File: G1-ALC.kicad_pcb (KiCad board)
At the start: 2 copper layers, 100 x 100.1 mm, 89 parts, among them J101 Conn_01x03_Pin, J102 330 VAC In, J103 G1 connections, J104 105VAC in, J105 Conn_01x03_Pin, J107 Conn_01x05_Pin, J108 G2 Control board interconnect, Q101 TIP122, U101 LM7812_TO220, U102 LM324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

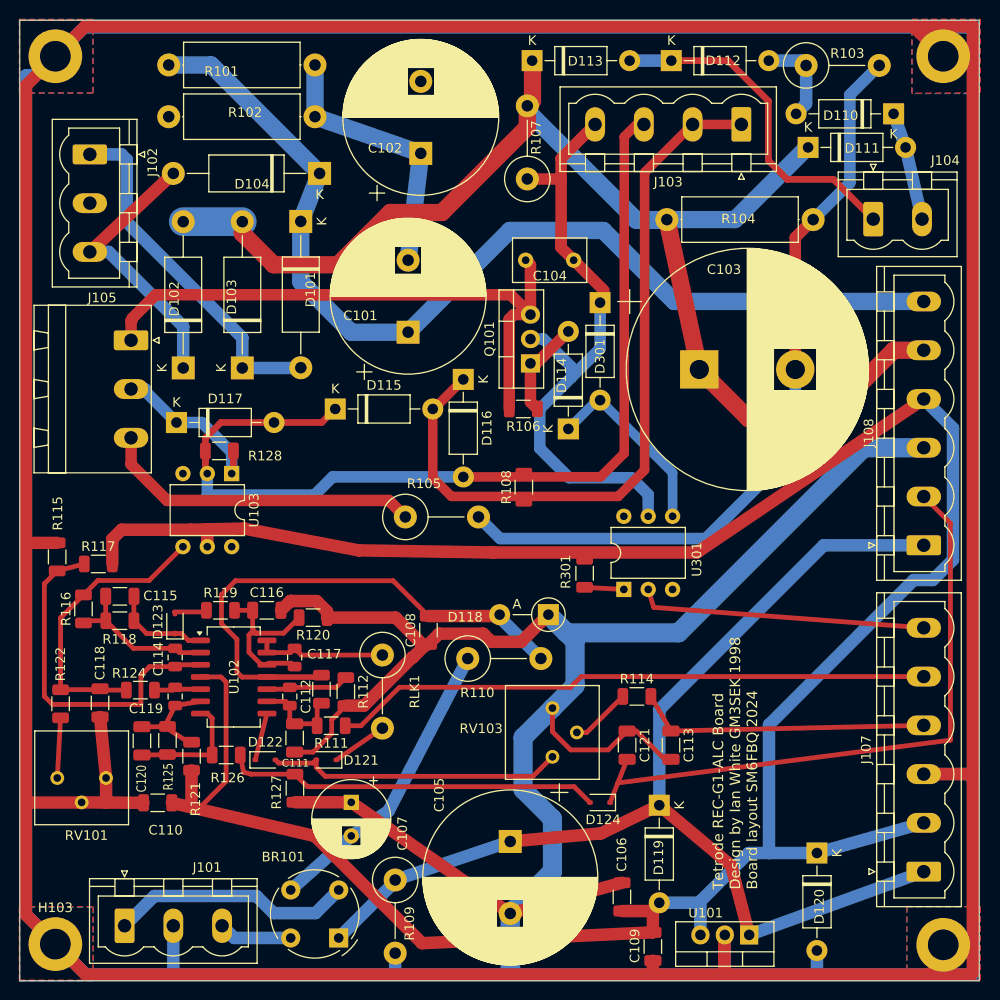
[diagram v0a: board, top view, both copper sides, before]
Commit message: Fixes for issues #1, #2, #3 and #4
Fixed unconnected capacitor and bleeder
Turned connectors around to orient screw connectors with screws outward from the board.
Use new footprint for BY228 diodes with larget pand and holes.
Moved components to make more room for the Q101 heat sink.
Cleared the top copper layer below the Q101 heat sink forn connected traces.
Added a copper zone below the Q101 heat sink to make it possible to solder the heat sink onto the board.
Opened the solder mask below the heat sink.

Added danger zones on both silkscreen layers. Along with warning texts.
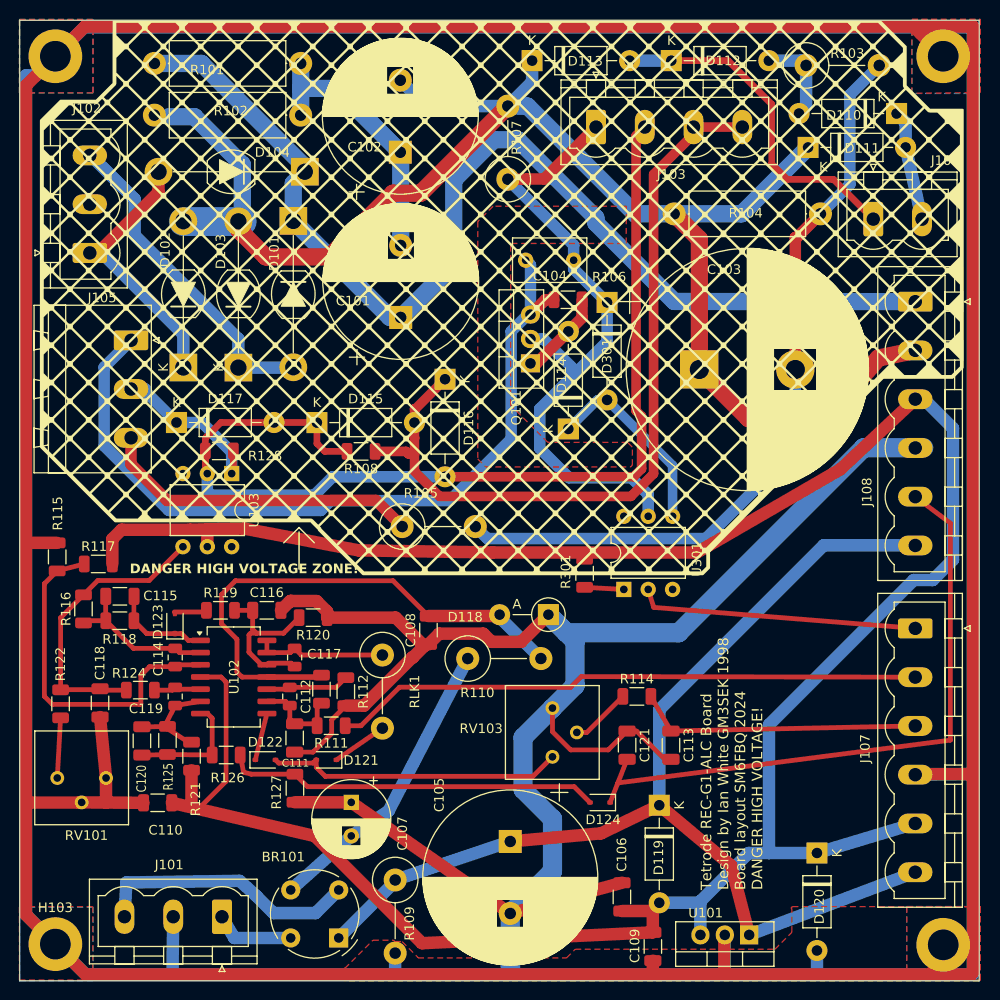
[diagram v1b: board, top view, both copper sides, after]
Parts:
- D101, D102, D103, D104: footprint Diode_THT:D_DO-15_P15.24mm_Horizontal -> Diode_THT_AKL:D_SOD-64_P15.24mm_big_holes_Horizontal
- moved J108 25.4 mm to (143.3, 54.3), turned to -90 degrees
- moved J107 25.4 mm to (143.3, 88.4), turned to -90 degrees
- moved R108 17.4 mm to (85.6, 69.9), turned to 180 degrees
- moved J103 15.1 mm to (110.1, 36.1), turned to 0 degrees
- moved R106 12.3 mm to (107.2, 54.1)
- moved J102 10.3 mm to (57.3, 49.2), turned to 90 degrees
- moved J101 10.2 mm to (71.1, 118.4), turned to 180 degrees
- moved D115 2.38 mm to (81.0, 66.9)
- moved C102 2.13 mm to (89.7, 38.8)
- moved R107 2.03 mm to (100.9, 41.6)
- moved D116 1.90 mm to (94.3, 62.4)
- moved C101 1.72 mm to (89.7, 56.0)
- moved R101 1.50 mm to (64.1, 29.5)
- moved D104 1.50 mm to (79.8, 40.8)
- moved R102 1.50 mm to (79.3, 34.9)
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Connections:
- C102 pad 2: unconnected-(C102-Pad2) -> /Cathode
- J101 pad 1: /18 VAC - -> /18 VAC +
- J101 pad 3: /18 VAC + -> /18 VAC -
- J102 pad 1: /330VAC - -> /330VAC +
- J102 pad 3: /330VAC + -> /330VAC -
- J103 pad 1: /G1 meter - -> /G1 Switch
- J103 pad 2: /G1 meter - -> /G1 meter +
- J103 pad 3: /G1 meter + -> /G1 meter -
- J103 pad 4: /G1 Switch -> /G1 meter -
- J107 pad 1: +24V -> Class AB1_L
- J107 pad 2: +12V -> INH IN
- J107 pad 3: GNDPWR -> ALC Out
- J107 pad 4: ALC Out -> GNDPWR
- J107 pad 5: INH IN -> +12V
- J107 pad 6: Class AB1_L -> +24V
- J108 pad 1: +24V -> /G2-Unreg
- J108 pad 2: /G1 current trip -> /Cathode
- J108 pad 3: GNDPWR -> +12V
- J108 pad 4: +12V -> GNDPWR
- J108 pad 5: /Cathode -> /G1 current trip
- J108 pad 6: /G2-Unreg -> +24V
- R102 pad 2: unconnected-(R102-Pad2) -> /Cathode
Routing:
- net /Cathode: track 136.7 -> 161.5 mm
- net /RV102 Cold: track 63.2 -> 83.1 mm
- net /G2-Unreg: track 106.6 -> 114.8 mm
- net /G1 meter +: track 101.6 -> 107.3 mm
- net /G1 meter -: track 78.7 -> 84.4 mm
- net /G1 Switch: track 64.1 -> 68.8 mm
- net /18 VAC -: track 25.3 -> 28.0 mm
- net /330VAC -: track 36.8 -> 34.3 mm
- net /330VAC +: track 29.2 -> 27.7 mm
- net +12V: track 267.5 -> 266.1 mm
- net GNDPWR: track 1030.2 -> 1031.6 mm
- net Net-(D114-A): track 10.4 -> 9.21 mm
- net ALC Out: track 30.5 -> 29.6 mm
- net INH IN: track 62.4 -> 61.5 mm
- net Class AB1_L: track 30.2 -> 29.3 mm
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- added copper zone on F.Cu, net (none)
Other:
- board text added: "DANGER HIGH VOLTAGE ZONE!"
- board text added: "DANGER! HIGH VOLTAGE ZONE"
- board text added: "Tetrode REC-G1-ALC Board Design by Ian White GM3SEK 1998 Board layout SM6FBQ 2024 DANGER HIGH VOLTAGE!"
- board text removed: "Tetrode REC-G1-ALC Board Design by Ian White GM3SEK 1998 Board layout SM6FBQ 2024"

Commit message: Added release number to the top silkscreen text.
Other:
- board text added: "Tetrode REC-G1-ALC Board Rel. 1.1 Design by Ian White GM3SEK 1998 Board layout SM6FBQ 2024 DANGER HIGH VOLTAGE!"
- board text removed: "Tetrode REC-G1-ALC Board Design by Ian White GM3SEK 1998 Board layout SM6FBQ 2024 DANGER HIGH VOLTAGE!"
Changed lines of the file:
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@@
 		)
 	)
-	(gr_text "Tetrode REC-G1-ALC Board\nDesign by Ian White GM3SEK 1998\nBoard layout SM6FBQ 2024\nDANGER HIGH VOLTAGE!"
+	(gr_text "Tetrode REC-G1-ALC Board Rel. 1.1\nDesign by Ian White GM3SEK 1998\nBoard layout SM6FBQ 2024\nDANGER HIGH VOLTAGE!"
 		(at 127.53 115.62 90)
 		(layer "F.SilkS")

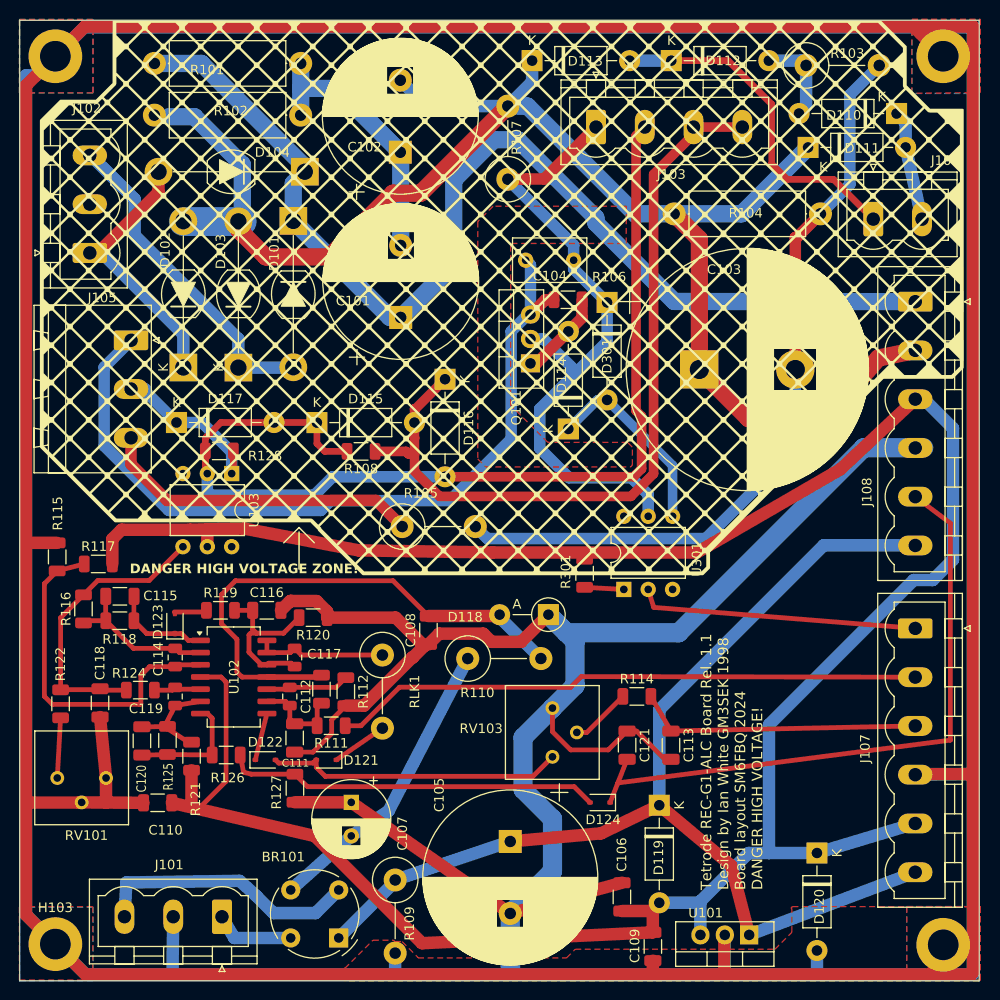
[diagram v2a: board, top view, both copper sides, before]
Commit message: Update connector positions and routing in G1-ALC.kicad_pcb
Repositioned two Phoenix Contact connectors in the PCB layout and rerouted the associated traces accordingly. Additionally rotated some properties at F.Fab layer to -90 degrees from the previous position at 270 degrees. Updated and added several segments in both B.Cu and F.Cu layers for better routing efficiency.
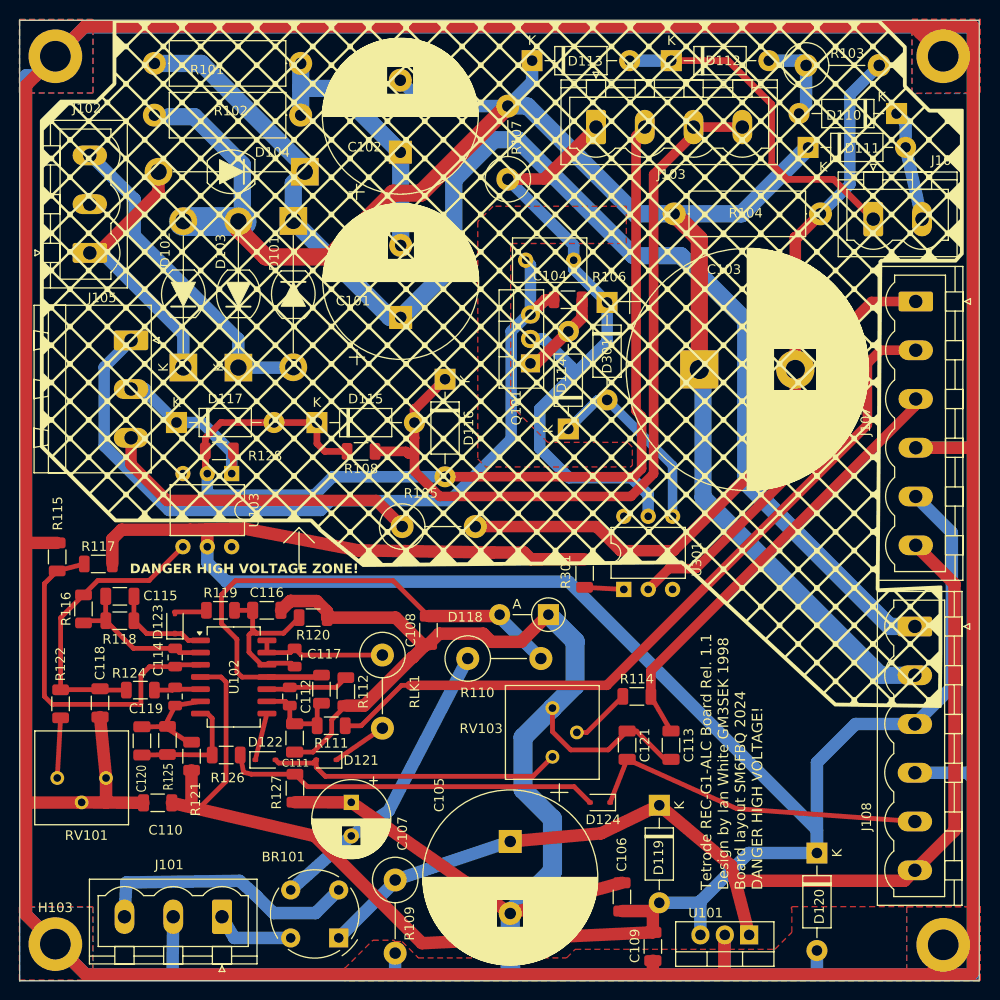
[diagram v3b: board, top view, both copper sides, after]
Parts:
- moved J107 34.1 mm to (143.4, 54.3)
- moved J108 33.8 mm to (143.3, 88.2)
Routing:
- net GNDPWR: track 1031.6 -> 990.7 mm
- net /G1 current trip: track 67.0 -> 36.0 mm
- net /G2-Unreg: track 114.8 -> 138.4 mm
- net +12V: track 266.1 -> 285.6 mm
- net INH IN: track 61.5 -> 79.4 mm
- net ALC Out: track 29.6 -> 46.6 mm
- net Class AB1_L: track 29.3 -> 45.9 mm
- net /Cathode: track 161.5 -> 176.6 mm
- net +24V: track 117.5 -> 110.9 mm

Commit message: Updated junction positions and wire connections in schematic
Performed major modifications to the junction positions and wire connections in the kicad schematic G1-ALC. The changes include removal and addition of certain junction points, repositioning of wires and altering electrical connections to improve schematic efficiency and accuracy.
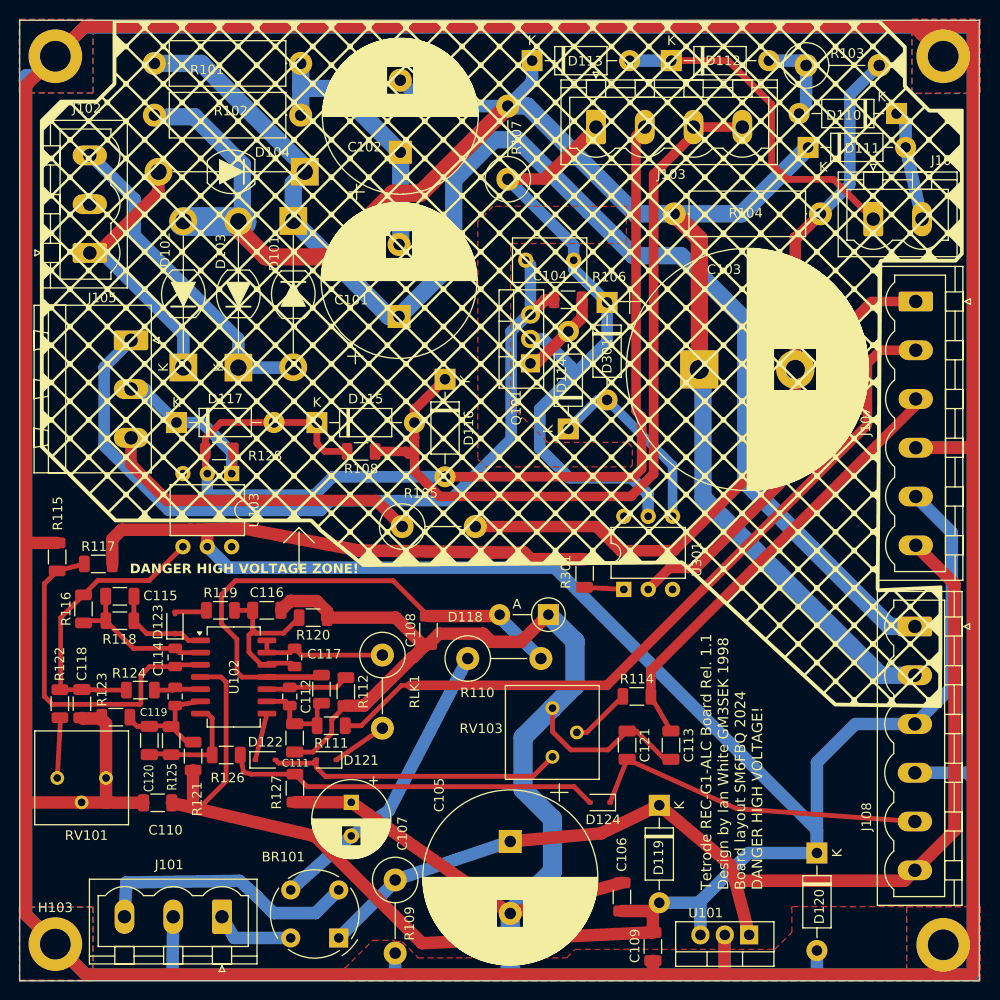
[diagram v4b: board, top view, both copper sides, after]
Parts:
- added R123: 22k, Resistor_SMD:R_1206_3216Metric, F.Cu at (60.0, 97.6)
- R108: value 1k5 -> Meter Shunt
- R128: value 1k5 -> 22k
- moved C118 1.89 mm to (56.5, 96.2)
- moved C120 0.77 mm to (63.5, 100.0)
- moved R125 0.39 mm to (65.8, 100.0)
- moved C101 0.20 mm to (89.6, 55.9)
- moved R121 0.16 mm to (68.1, 101.7)
- moved R122 0.08 mm to (54.2, 96.2)
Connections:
- net +12V renamed +12V Reg
- net +24V renamed +24V Unreg
- net /G1 current trip renamed /G1 trip
- net /G2-Unreg renamed /G2 Unreg
- net INH IN renamed /Inhibit
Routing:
- net GNDPWR: track 990.7 -> 992.8 mm
- net Net-(U102B--): track 10.8 -> 12.6 mm

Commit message: Changed optocoupler U103 to a MCT5211
The optocoupler U103 must be as sensitive as the MCT5211. It could not be replaced by CNY17-4 despite what is said by Mouser when searching for the MCT5211. Fortunately DigiKey has a direct replacement with the same specifications: MCT5211M.
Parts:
- U103: value CNY17-4 -> MCT5211M
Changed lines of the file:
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@@
 			)
 		)
-		(property "Datasheet" "http://www.vishay.com/docs/83606/cny17.pdf"
+		(property "Datasheet" "https://www.vishay.com/docs/83606/cny17.pdf"
 			(at 0 0 90)
 			(unlocked yes)
@@
 			)
 		)
-		(property "Description" ""
+		(property "Description" "Optoisolator Transistor with Base Output "
 			(at 0 0 90)
 			(unlocked yes)
@@
 			)
 		)
-		(property "Order #" "40301704"
+		(property "Order #" "751-1268-5-ND"
 			(at 0 0 0)
 			(layer "F.Fab")
@@
 			)
 		)
-		(property "Supplier" "Electrokit"
+		(property "Supplier" "DigiKey"
 			(at 0 0 0)
 			(layer "F.Fab")
@@
 			)
 		)
-		(property "Value" "CNY17-4"
+		(property "Value" "MCT5211M"
 			(at 3.81 7.41 90)
 			(layer "F.Fab")
@@
 			)
 		)
-		(property "Datasheet" "http://www.vishay.com/docs/83606/cny17.pdf"
+		(property "Datasheet" "https://www.onsemi.com/pdf/datasheet/mct5211m-d.pdf"
 			(at 0 0 -90)
 			(unlocked yes)
@@
 			)
 		)
-		(property "Description" ""
+		(property "Description" "Optoisolator Transistor with Base Output 4170Vrms 1 Channel 6-DIP CTR 110%@1mA"
 			(at 0 0 -90)
 			(unlocked yes)
@@
 			)
 		)
-		(property "Notes" ""
+		(property "Notes" "This component is crucial. It cannot simply be exchanged for any other optocoupler because its sensititity to low LED current is needed."
 			(at 0 0 0)
 			(layer "F.Fab")
@@
 			)
 		)
-		(property "Order #" "40301704"
+		(property "Order #" "MCT5211M-ND"
 			(at 0 0 0)
 			(layer "F.Fab")
@@
 			)
 		)
-		(property "Supplier" "Electrokit"
+		(property "Supplier" "DigiKey"
 			(at 0 0 0)
 			(layer "F.Fab")
@@
 		)
 		(property "Value" "22k"
-			(at 0 1.82 360)
+			(at 0 1.82 0)
 			(layer "F.Fab")
 			(effects
@@
 		)
 		(fp_text user "${REFERENCE}"
-			(at 0 0 360)
+			(at 0 0 0)
 			(layer "F.Fab")
 			(effects

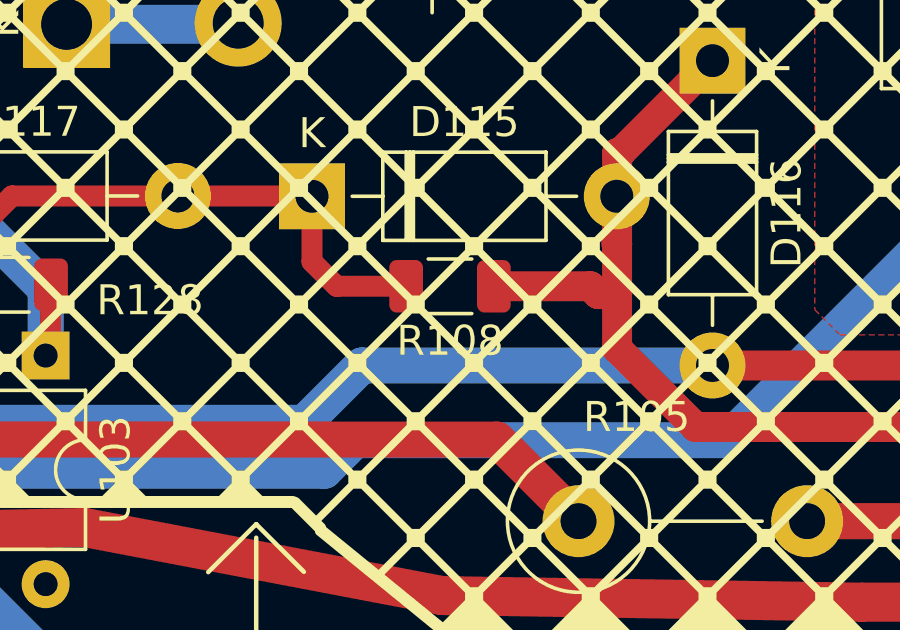
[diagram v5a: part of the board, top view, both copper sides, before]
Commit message: Cleanup schematic. No functional change.
Replaced global labels with hierarchical.
Consistent placement of references and values.
Values typed in a smaller font.
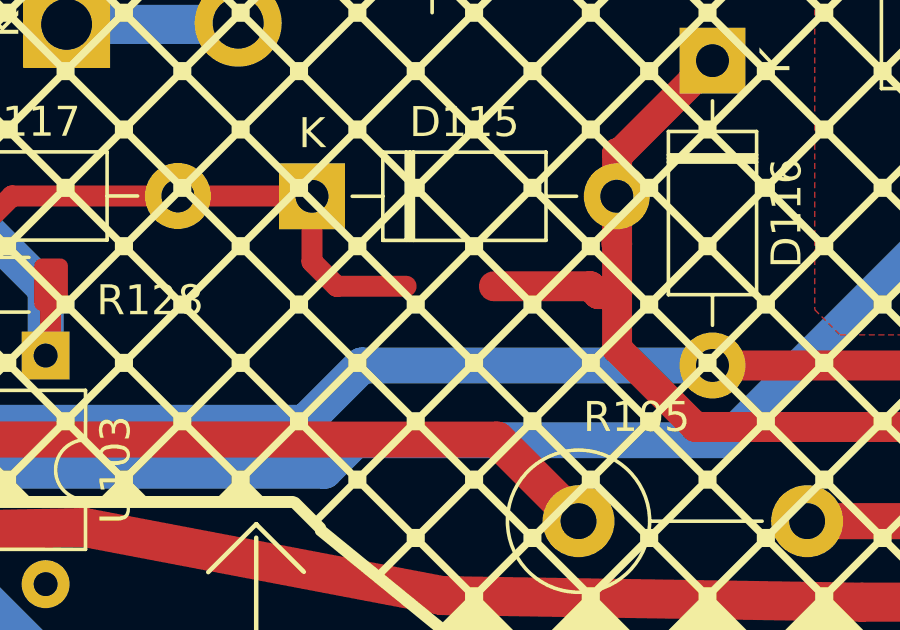
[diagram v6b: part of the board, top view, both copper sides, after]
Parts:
- removed R108: Meter Shunt, Resistor_SMD:R_1206_3216Metric
- C116: value 1u0 -> 1u
- J103: value G1 connections -> G1 conn.
- R120: value 1M0 -> 1M
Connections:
- net /G1 meter - renamed /G1
- net /RV102 HOT renamed /RV102 Hot
- net /RV102 MID renamed /RV102 Mid
- net ALC Out renamed /ALC
- net Class AB1_L renamed /Class AB1_L
